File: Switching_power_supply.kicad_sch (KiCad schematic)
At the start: 20 parts, among them J10 Conn_01x02, J11 Conn_01x02, J5 Conn_01x03_Pin, J8 Conn_01x02, J9 Conn_01x02, U2 LM2596HVS-ADJRG, U3 AMS1117

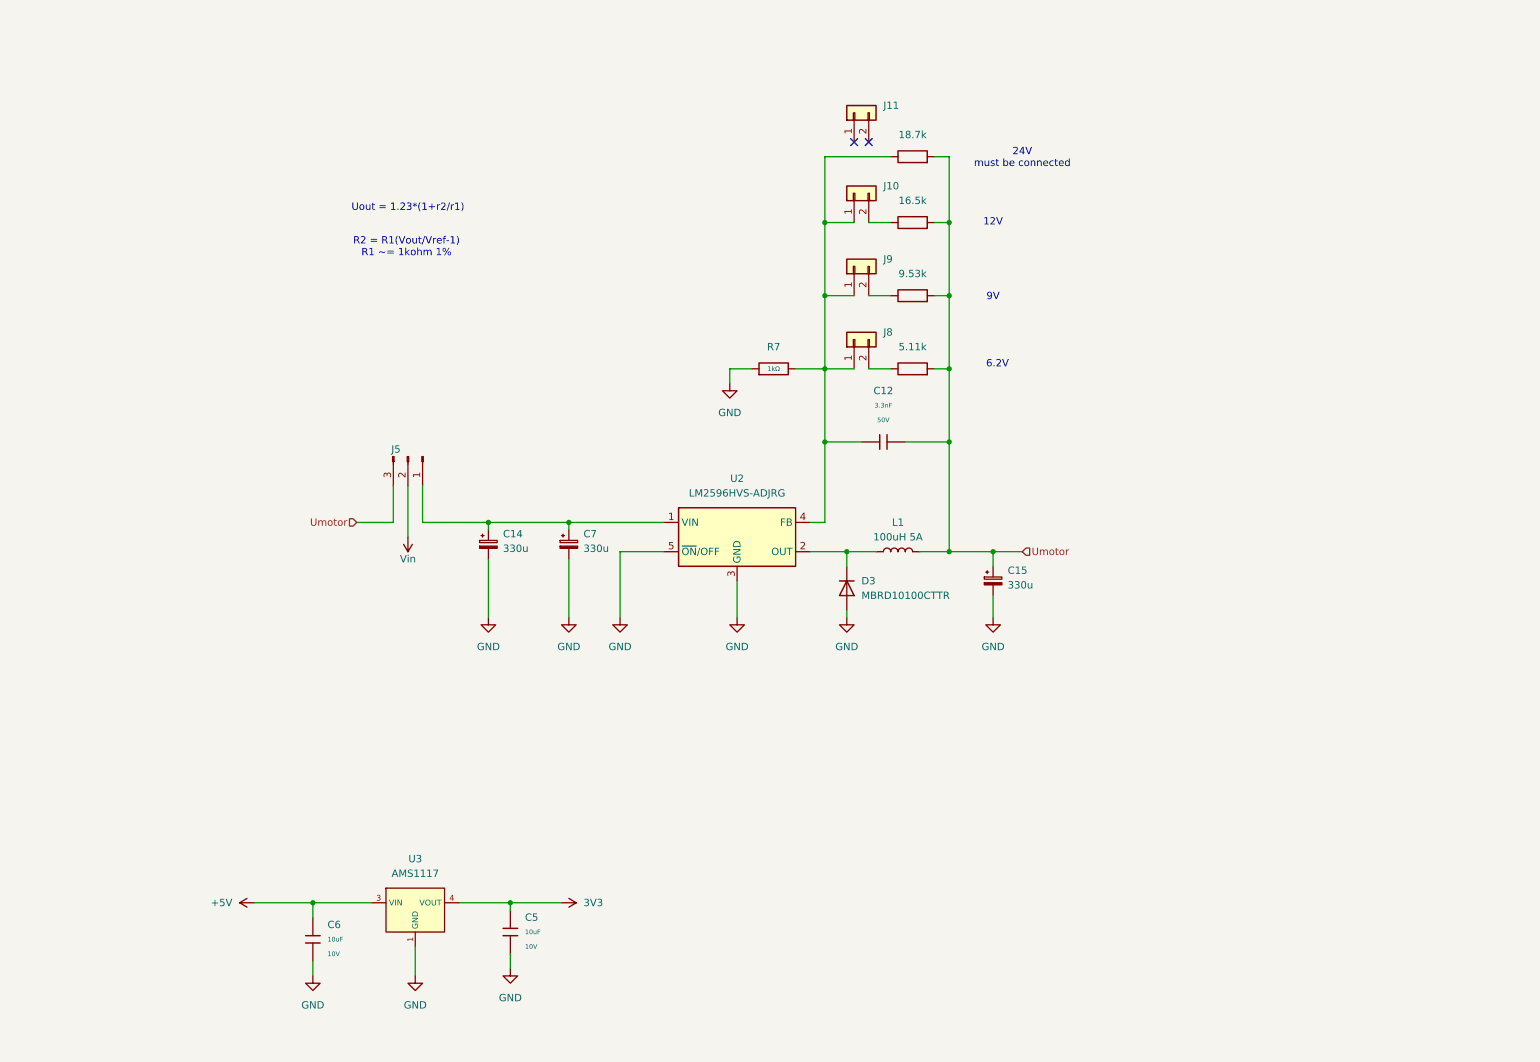
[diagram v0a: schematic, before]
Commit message: finished schematic (without some part numbers)
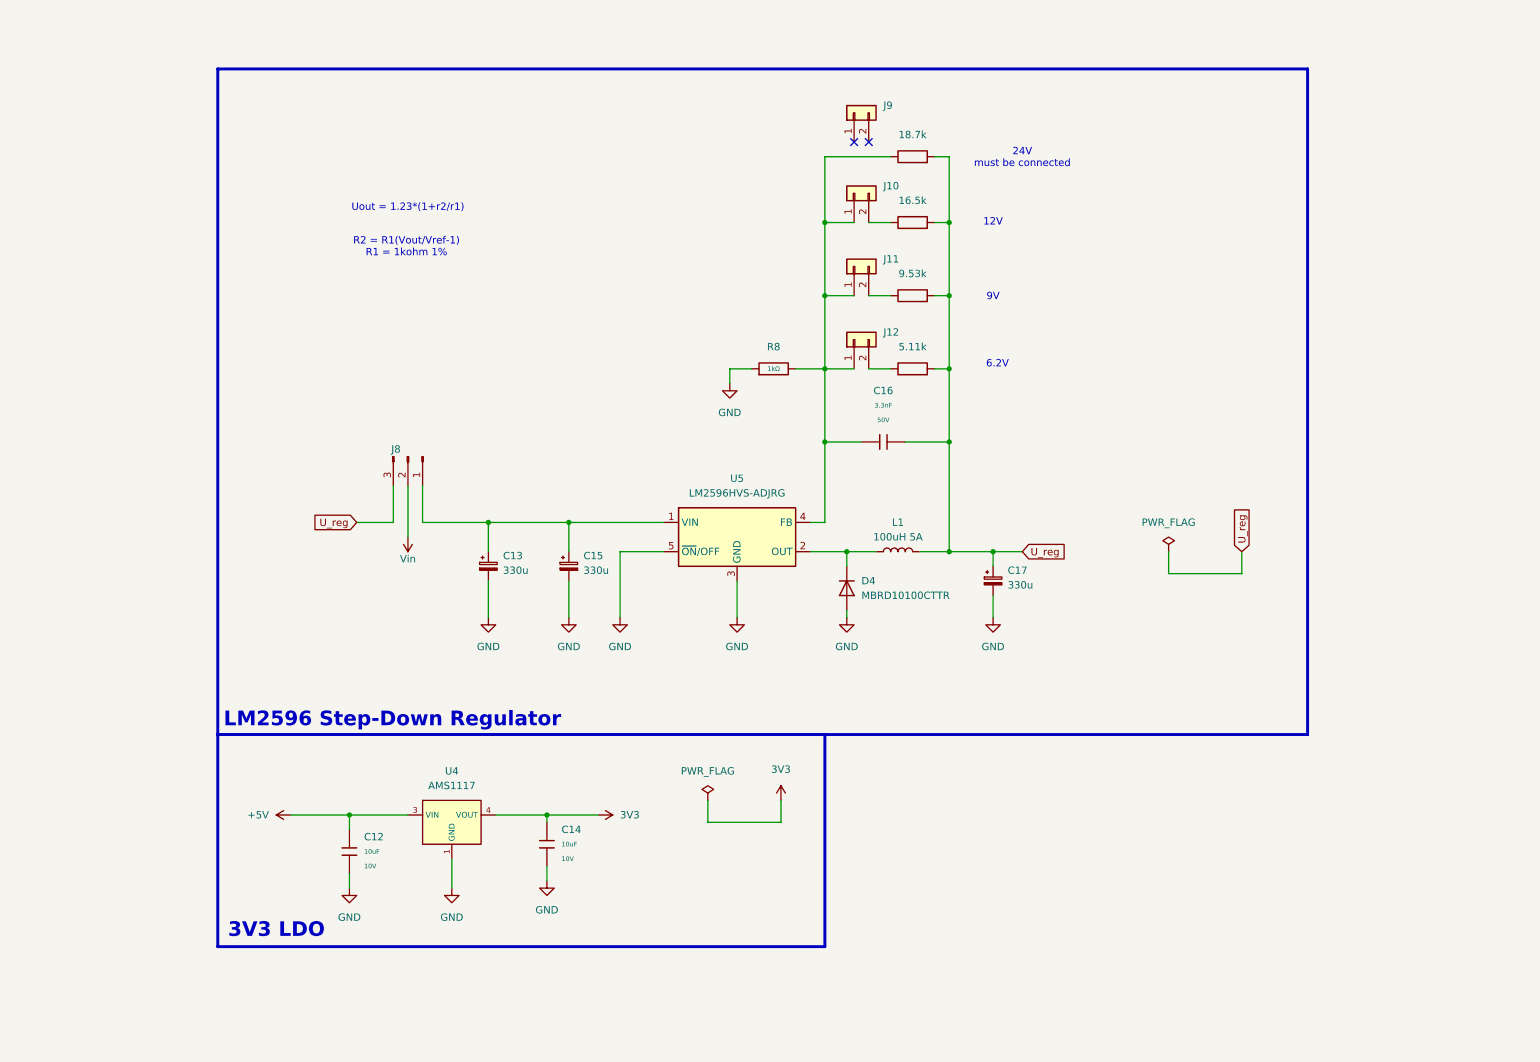
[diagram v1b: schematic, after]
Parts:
- renumbered C6 to C12, C14 to C13, C5 to C14, C7 to C15, C12 to C16, C15 to C17, D3 to D4, J9 to J11, J8 to J12, J5 to J8, J11 to J9, R5 to R10, R4 to R11, R2 to R12, R7 to R8, R6 to R9, U3 to U4, U2 to U5
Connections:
- net Umotor renamed U_reg
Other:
- note added: "3V3 LDO"
- note added: "LM2596 Step-Down Regulator"
- note added: "R2 = R1(Vout/Vref-1) R1 = 1kohm 1%"
- note removed: "R2 = R1(Vout/Vref-1) R1 ~= 1kohm 1%"
- moved on the sheet: C12, C13, C14, C15, U4

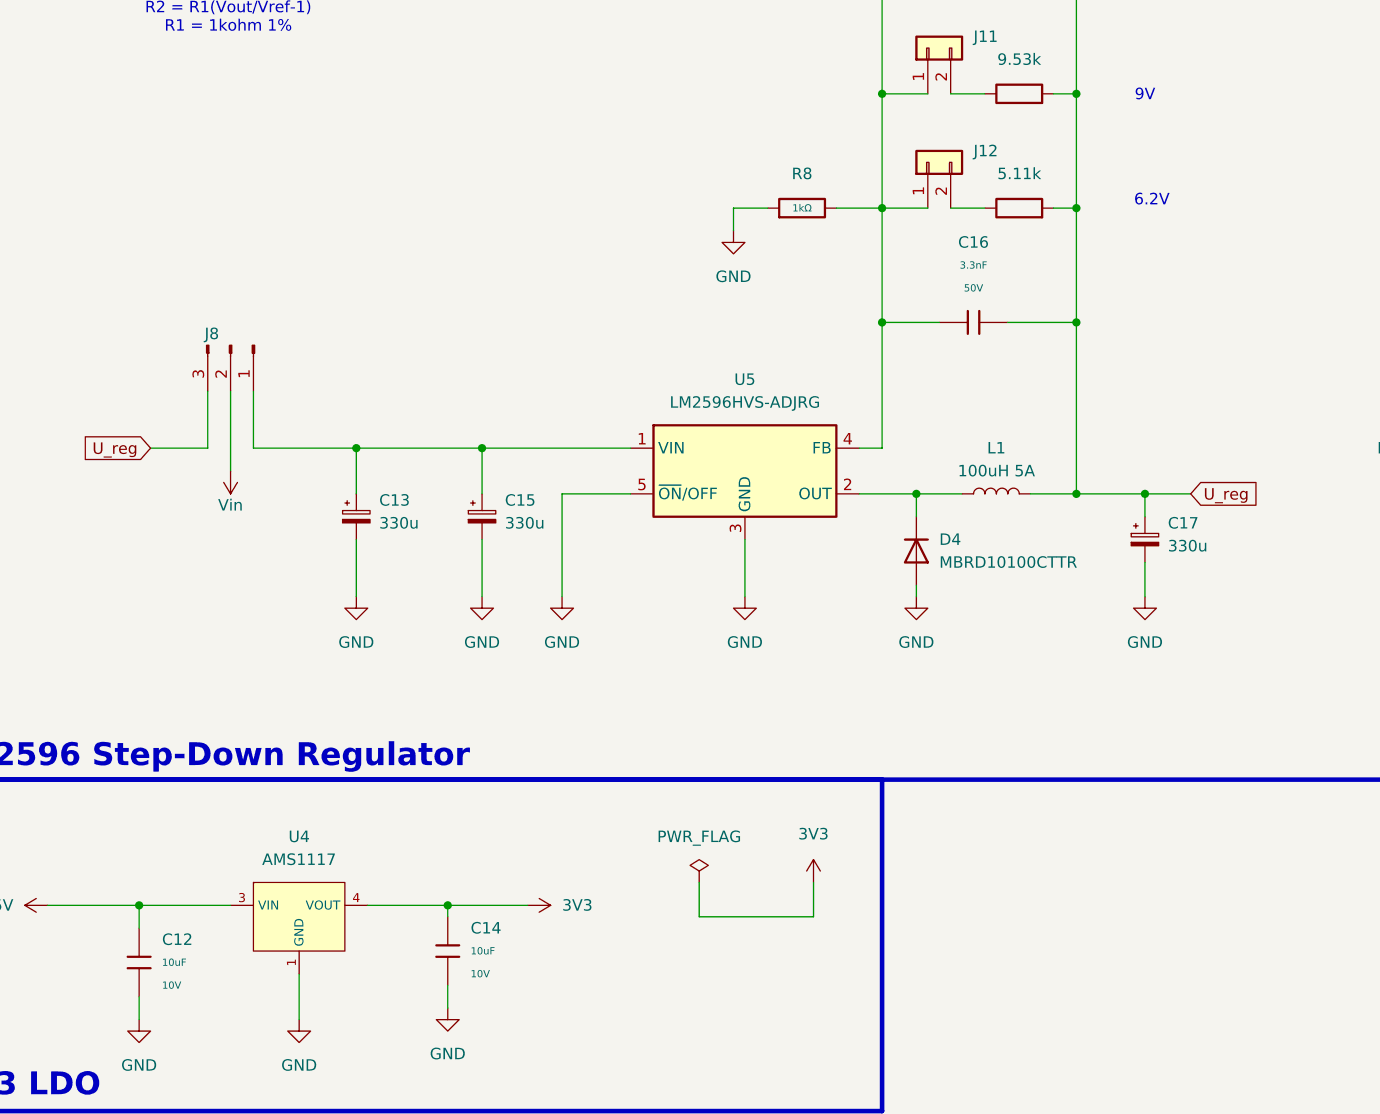
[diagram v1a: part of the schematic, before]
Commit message: initial component placement
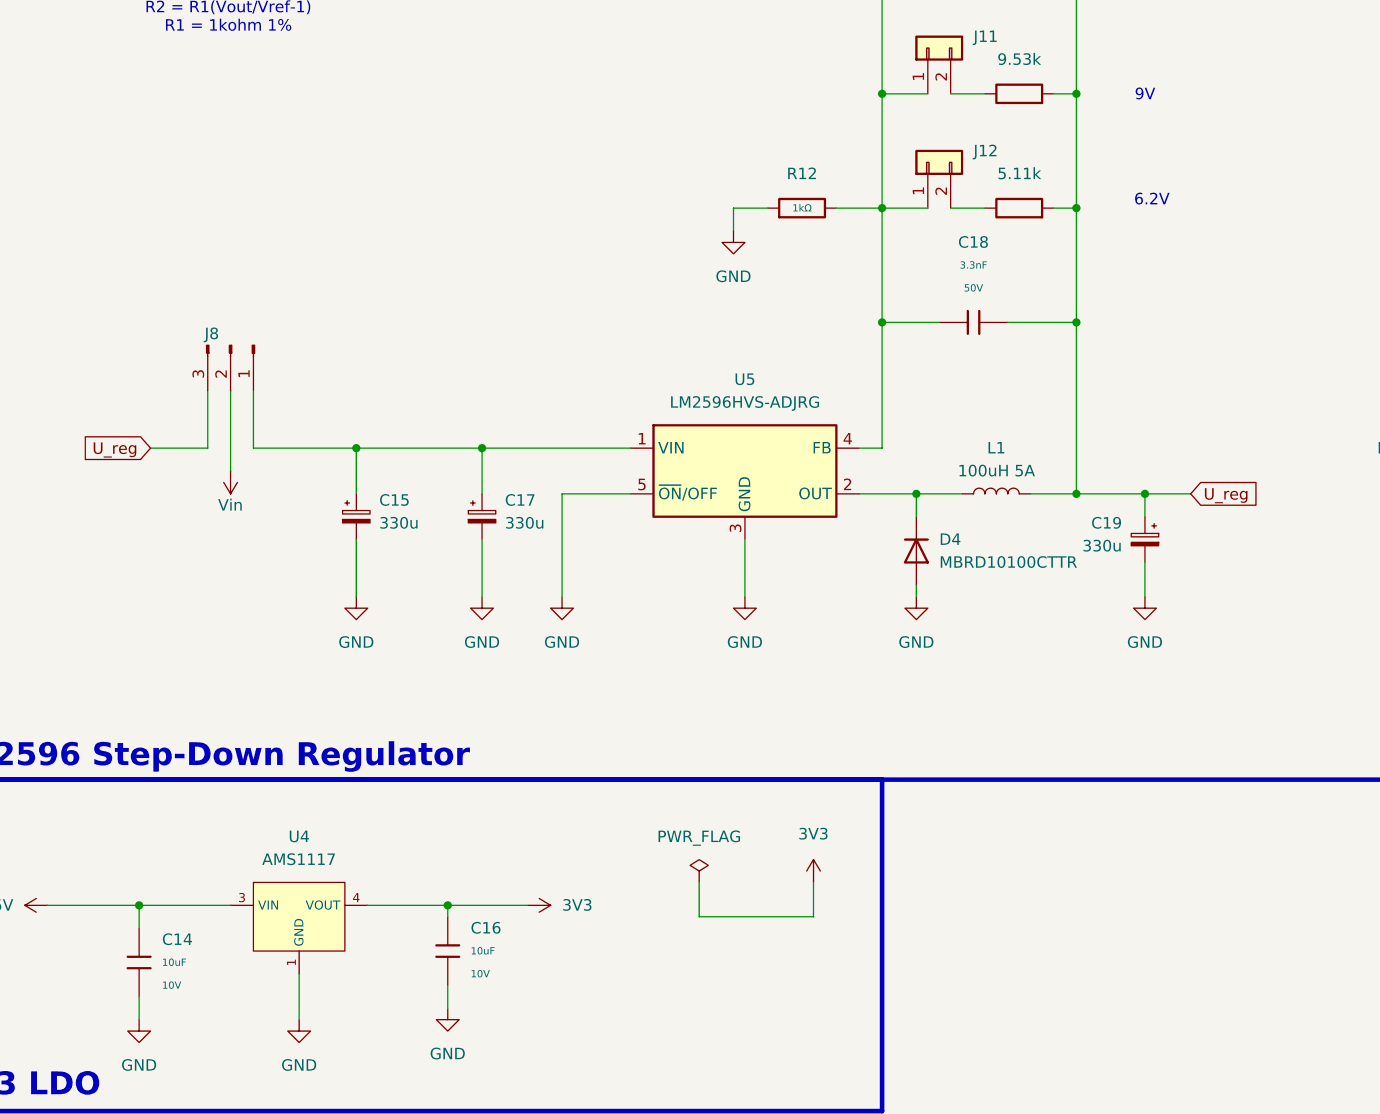
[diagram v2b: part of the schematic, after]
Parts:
- C15: renamed from C13; footprint (none) -> Capacitor_THT:CP_Radial_D12.5mm_P5.00mm
- C17: renamed from C15; footprint (none) -> Capacitor_THT:CP_Radial_D12.5mm_P5.00mm
- C19: renamed from C17; footprint (none) -> Capacitor_SMD:CP_Elec_18x17.5
- D4: footprint (none) -> Package_TO_SOT_SMD:TO-252-2
- J10, J12, J9: footprint (none) -> Connector_PinHeader_2.54mm:PinHeader_1x02_P2.54mm_Vertical_SMD_Pin1Right
- J11: value Conn_01x02 -> ~; footprint (none) -> Connector_PinHeader_2.54mm:PinHeader_1x02_P2.54mm_Vertical_SMD_Pin1Right
- J8: footprint (none) -> Connector_PinHeader_2.54mm:PinHeader_1x03_P2.54mm_Vertical
- L1: footprint (none) -> Inductor_THT:L_Toroid_Vertical_L21.6mm_W11.4mm_P7.62mm_Pulse_KM-3
- R13: renamed from R9; footprint (none) -> PCM_JLCPCB:R_0402; LCSC (none) -> RC0402FR-0710KL
- R14: renamed from R10; footprint (none) -> PCM_JLCPCB:R_0402; LCSC (none) -> FRC0402F1652TS
- R15: renamed from R11; footprint (none) -> PCM_JLCPCB:R_0402; LCSC (none) -> C295883
- R16: renamed from R12; footprint (none) -> PCM_JLCPCB:R_0402; LCSC (none) -> C274895
- renumbered C12 to C14, C14 to C16, C16 to C18, R8 to R12

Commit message: revision
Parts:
- removed C15, C17: 330u, Capacitor_THT:CP_Radial_D12.5mm_P5.00mm, symbol Device:C_Polarized_Small
- removed C19: 330u, Capacitor_SMD:CP_Elec_18x17.5, symbol Device:C_Polarized_Small
- removed D4: MBRD10100CTTR, Package_TO_SOT_SMD:TO-252-2, symbol Device:D
- added C18, C19, C21, C22: 100nF, PCM_JLCPCB:C_0603, symbol PCM_JLCPCB-Capacitors:0603,100nF
- added D5: MBRD10100CTTR, SMC_MBRD10100CTTR:TO-252-3_L6.5-W5.8-P4.58-TL, symbol SMC_MBRD10100CTTR:MBRD10100CTTR
- added R10, R11, R17, R18: 33kΩ, PCM_JLCPCB:R_0402, symbol PCM_JLCPCB-Resistors:0402,33kΩ
- J10, J12, J9: footprint Connector_PinHeader_2.54mm:PinHeader_1x02_P2.54mm_Vertical_SMD_Pin1Right -> Connector_PinHeader_2.54mm:PinHeader_1x02_P2.54mm_Vertical
- J11: value ~ -> Conn_01x02; footprint Connector_PinHeader_2.54mm:PinHeader_1x02_P2.54mm_Vertical_SMD_Pin1Right -> Connector_PinHeader_2.54mm:PinHeader_1x02_P2.54mm_Vertical
- R13: LCSC RC0402FR-0710KL -> C11476
- R14: LCSC FRC0402F1652TS -> C25857
- renumbered C14 to C16, C16 to C17, C18 to C20
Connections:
- net GND: now also C19.2, C22.2, D5.1, D5.3, R11.2, R18.2
- net U_reg: now also C21.1, R17.1
- net at L1.1, U5.2 (OUT): now also D5.2 (K)
- net at J8.1 (Pin_1), U5.1 (VIN): now also C18.1, R10.1
- net 3V3 renamed +3V3
- new net: C18.2, C19.1, R10.2, R11.1
- new net: C21.2, C22.1, R17.2, R18.1
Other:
- moved on the sheet: C16, C17, J8, U4

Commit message: second component placement
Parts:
- added C17, C19, C25, C26, C27, C28: 47u, Capacitor_SMD:CP_Elec_6.3x7.7, symbol Device:C_Polarized_Small
- J10, J11, J12, J9: footprint Connector_PinHeader_2.54mm:PinHeader_1x02_P2.54mm_Vertical -> Connector_PinHeader_2.54mm:PinHeader_1x02_P2.54mm_Horizontal
- L1: value 100uH 5A -> 100uH 4A; footprint Inductor_THT:L_Toroid_Vertical_L21.6mm_W11.4mm_P7.62mm_Pulse_KM-3 -> Inductor_SMD:L_APV_APH1265; LCSC C3007746 -> C20415559
- renumbered C17 to C18, C18 to C20, C19 to C21, C20 to C22, C21 to C23, C22 to C24, D5 to D4
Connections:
- net GND: now also C17.2, C19.2, C25.2, C26.2, C27.2, C28.2
- net U_reg: now also C25.1, C26.1, C28.1
- net at C20.1, J8.1 (Pin_1), R10.1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: now also C17.1, C19.1, C27.1
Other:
- note added: "Connect 2-1 To use regulator 2-3 To bypas regulator and use Vin directly"

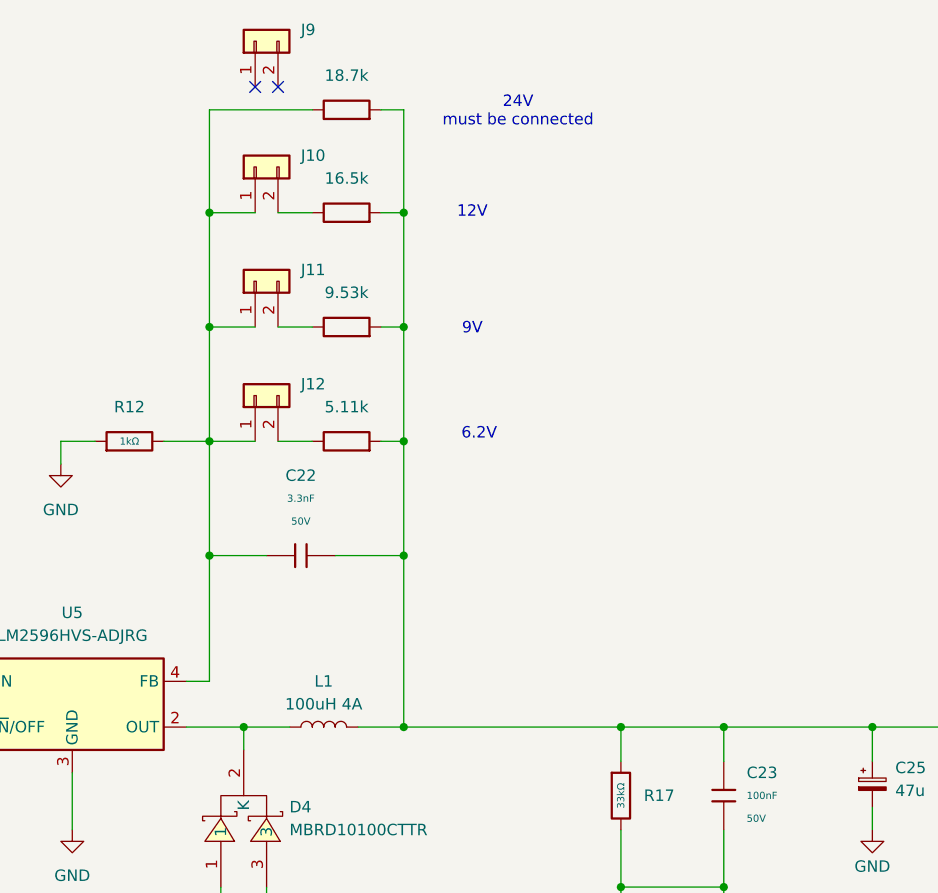
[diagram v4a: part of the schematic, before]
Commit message: Added design rules to PCB and updated dip switch
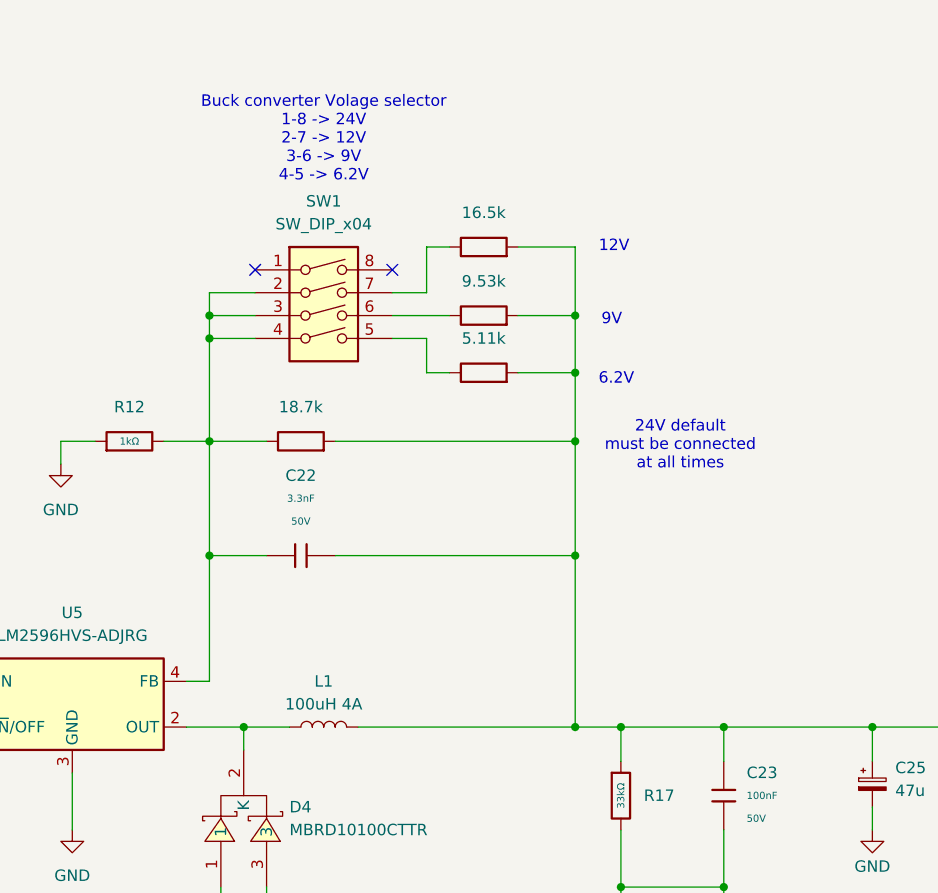
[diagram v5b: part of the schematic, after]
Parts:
- removed J10, J11, J12, J9: Conn_01x02, Connector_PinHeader_2.54mm:PinHeader_1x02_P2.54mm_Horizontal, symbol Connector_Generic:Conn_01x02
- added SW1: SW_DIP_x04, Button_Switch_THT:SW_DIP_SPSTx04_Slide_6.7x11.72mm_W7.62mm_P2.54mm_LowProfile, symbol Switch:SW_DIP_x04
- L1: footprint Inductor_SMD:L_APV_APH1265 -> Inductor_SMD:L_Sunlord_SWRB1207S; LCSC C20415559 -> C5368704
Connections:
- net at C22.1, R12.2, R13.1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: now also SW1.2, SW1.3, SW1.4
- net at R16.1: now also SW1.5
- net at R15.1: now also SW1.6
- net at R14.1: now also SW1.7
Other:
- note added: "24V default must be connected at all times"
- note added: "Buck converter Volage selector 1-8 -> 24V 2-7 -> 12V 3-6 -> 9V 4-5 -> 6.2V"
- note removed: "24V must be connected"
